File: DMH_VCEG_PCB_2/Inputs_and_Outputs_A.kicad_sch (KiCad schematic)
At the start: 43 parts, among them J1 TS_Jack_6.35mm_Sw, J10 TS_Jack_6.35mm_Sw, J2 TS_Jack_6.35mm_Sw, J200 IDC_02x08, J21 Conn_01x10_PinHeader, J22 Conn_01x10_PinHeader, J23 Conn_01x10_PinHeader, J24 Conn_01x06_PinHeader, J3 TS_Jack_6.35mm_Sw, J4 TS_Jack_6.35mm_Sw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

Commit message: Synced changes to PCB 2
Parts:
- added R197: 68k, Resistor_THT:R_Axial_DIN0207_L6.3mm_D2.5mm_P7.62mm_Horizontal, symbol Device:R_US
- added R198: 100k, Resistor_THT:R_Axial_DIN0207_L6.3mm_D2.5mm_P7.62mm_Horizontal, symbol Device:R_US
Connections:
- net +12V: now also R197.1
- net GND: now also R198.2; no longer U8.12 (+)
- new net: R197.2, R198.1, U8.12 (+)
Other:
- moved on the sheet: R88, U8D

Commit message: PCB 2 routing in progress
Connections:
- net Att CV A: no longer J23.3 (Pin_3)
- net Dec CV A: no longer J23.6 (Pin_6)
- net Rel CV A: no longer J23.10 (Pin_10)
- net Sus CV A: no longer J23.7 (Pin_7)
- no-connect marks 1 -> 5
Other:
- moved on the sheet: J23C, J23F, J23G, J23J
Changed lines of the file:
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@@
 	)
 	(junction
-		(at 146.05 34.29)
-		(diameter 0)
-		(color 0 0 0 0)
-	)
-	(junction
 		(at 171.45 163.83)
 		(diameter 0)
@@
 	)
 	(junction
-		(at 146.05 129.54)
-		(diameter 0)
-		(color 0 0 0 0)
-	)
-	(junction
 		(at 86.36 273.05)
 		(diameter 0)
@@
 	)
 	(junction
-		(at 146.05 66.04)
-		(diameter 0)
-		(color 0 0 0 0)
-	)
-	(junction
 		(at 115.57 63.5)
 		(diameter 0)
@@
 	)
 	(junction
-		(at 146.05 97.79)
-		(diameter 0)
-		(color 0 0 0 0)
-	)
-	(junction
 		(at 88.9 127)
 		(diameter 0)
@@
 	)
 	(no_connect
+		(at 146.05 127)
+	)
+	(no_connect
+		(at 146.05 95.25)
+	)
+	(no_connect
+		(at 146.05 31.75)
+	)
+	(no_connect
 		(at 66.04 257.81)
 	)
+	(no_connect
+		(at 146.05 63.5)
+	)
 	(wire
 		(pts
-			(xy 138.43 34.29) (xy 146.05 34.29)
+			(xy 138.43 34.29) (xy 158.75 34.29)
 		)
 		(stroke
@@
 	(wire
 		(pts
-			(xy 146.05 129.54) (xy 158.75 129.54)
+			(xy 138.43 129.54) (xy 158.75 129.54)
 		)
 		(stroke
@@
 	(wire
 		(pts
-			(xy 146.05 34.29) (xy 158.75 34.29)
-		)
-		(stroke
-			(width 0)
-			(type default)
-		)
-	)
-	(wire
-		(pts
 			(xy 152.4 246.38) (xy 176.53 246.38)
 		)
@@
 	(wire
 		(pts
-			(xy 138.43 129.54) (xy 146.05 129.54)
-		)
-		(stroke
-			(width 0)
-			(type default)
-		)
-	)
-	(wire
-		(pts
 			(xy 127 49.53) (xy 127 46.99)
 		)
@@
 	(wire
 		(pts
-			(xy 138.43 97.79) (xy 146.05 97.79)
-		)
-		(stroke
-			(width 0)
-			(type default)
-		)
-	)
-	(wire
-		(pts
-			(xy 138.43 66.04) (xy 146.05 66.04)
-		)
-		(stroke
-			(width 0)
-			(type default)
-		)
-	)
-	(wire
-		(pts
 			(xy 48.26 170.18) (xy 58.42 170.18)
 		)
@@
 	(wire
 		(pts
-			(xy 146.05 66.04) (xy 158.75 66.04)
+			(xy 138.43 66.04) (xy 158.75 66.04)
 		)
 		(stroke
@@
 	(wire
 		(pts
-			(xy 146.05 97.79) (xy 158.75 97.79)
+			(xy 138.43 97.79) (xy 158.75 97.79)
 		)
 		(stroke
@@
 	(symbol
 		(lib_id "SynthStuff:Conn_01x10_PinHeader")
-		(at 146.05 124.46 270)
+		(at 146.05 121.92 270)
 		(unit 10)
 		(exclude_from_sim no)
@@
 		(fields_autoplaced yes)
 		(property "Reference" "J23"
-			(at 147.32 125.0949 90)
+			(at 147.32 122.5549 90)
 			(effects
 				(font
@@
 		)
 		(property "Value" "Conn_01x10_PinHeader"
-			(at 143.51 124.46 0)
+			(at 143.51 121.92 0)
 			(effects
 				(font
@@
 		)
 		(property "Footprint" "Connector_PinSocket_2.54mm:PinSocket_1x10_P2.54mm_Vertical"
-			(at 146.05 124.46 0)
+			(at 146.05 121.92 0)
 			(effects
 				(font
@@
 		)
 		(property "Datasheet" "~"
-			(at 146.05 124.46 0)
+			(at 146.05 121.92 0)
 			(effects
 				(font
@@
 		)
 		(property "Description" "Generic connector, single row, 01x10"
-			(at 146.05 124.46 0)
+			(at 146.05 121.92 0)
 			(effects
 				(font
@@
 	(symbol
 		(lib_id "SynthStuff:Conn_01x10_PinHeader")
-		(at 146.05 29.21 270)
+		(at 146.05 26.67 270)
 		(unit 3)
 		(exclude_from_sim no)
@@
 		(fields_autoplaced yes)
 		(property "Reference" "J23"
-			(at 147.32 29.8449 90)
+			(at 147.32 27.3049 90)
 			(effects
 				(font
@@
 		)
 		(property "Value" "Conn_01x10_PinHeader"
-			(at 143.51 29.21 0)
+			(at 143.51 26.67 0)
 			(effects
 				(font
@@
 		)
 		(property "Footprint" "Connector_PinSocket_2.54mm:PinSocket_1x10_P2.54mm_Vertical"
-			(at 146.05 29.21 0)
+			(at 146.05 26.67 0)
 			(effects
 				(font
@@
 		)
 		(property "Datasheet" "~"
-			(at 146.05 29.21 0)
+			(at 146.05 26.67 0)
 			(effects
 				(font
@@
 		)
 		(property "Description" "Generic connector, single row, 01x10"
-			(at 146.05 29.21 0)
+			(at 146.05 26.67 0)
 			(effects
 				(font
@@
 	(symbol
 		(lib_id "SynthStuff:Conn_01x10_PinHeader")
-		(at 146.05 60.96 270)
+		(at 146.05 58.42 270)
 		(unit 6)
 		(exclude_from_sim no)
@@
 		(fields_autoplaced yes)
 		(property "Reference" "J23"
-			(at 147.32 61.5949 90)
+			(at 147.32 59.0549 90)
 			(effects
 				(font
@@
 		)
 		(property "Value" "Conn_01x10_PinHeader"
-			(at 143.51 60.96 0)
+			(at 143.51 58.42 0)
 			(effects
 				(font
@@
 		)
 		(property "Footprint" "Connector_PinSocket_2.54mm:PinSocket_1x10_P2.54mm_Vertical"
-			(at 146.05 60.96 0)
+			(at 146.05 58.42 0)
 			(effects
 				(font
@@
 		)
 		(property "Datasheet" "~"
-			(at 146.05 60.96 0)
+			(at 146.05 58.42 0)
 			(effects
 				(font
@@
 		)
 		(property "Description" "Generic connector, single row, 01x10"
-			(at 146.05 60.96 0)
+			(at 146.05 58.42 0)
 			(effects
 				(font
@@
 	(symbol
 		(lib_id "SynthStuff:Conn_01x10_PinHeader")
-		(at 146.05 92.71 270)
+		(at 146.05 90.17 270)
 		(unit 7)
 		(exclude_from_sim no)
@@
 		(fields_autoplaced yes)
 		(property "Reference" "J23"
-			(at 147.32 93.3449 90)
+			(at 147.32 90.8049 90)
 			(effects
 				(font
@@
 		)
 		(property "Value" "Conn_01x10_PinHeader"
-			(at 143.51 92.71 0)
+			(at 143.51 90.17 0)
 			(effects
 				(font
@@
 		)
 		(property "Footprint" "Connector_PinSocket_2.54mm:PinSocket_1x10_P2.54mm_Vertical"
-			(at 146.05 92.71 0)
+			(at 146.05 90.17 0)
 			(effects
 				(font
@@
 		)
 		(property "Datasheet" "~"
-			(at 146.05 92.71 0)
+			(at 146.05 90.17 0)
 			(effects
 				(font
@@
 		)
 		(property "Description" "Generic connector, single row, 01x10"
-			(at 146.05 92.71 0)
+			(at 146.05 90.17 0)
 			(effects
 				(font

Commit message: Restarted component placing on Main
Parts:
- removed unit 10 of J23
- removed unit 3 of J23
- removed unit 6 of J23
- removed unit 7 of J23
- renumbered J23 to J22
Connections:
- net Rel CV A: now also U21.8; no longer U21.14
- net SG Out A: now also J22.4 (Pin_4); no longer J22.2 (Pin_2)
- net Sus CV A: now also U21.14; no longer U21.8
- net at RV18.2: now also U21.10 (+); no longer U21.12 (+)
- net at R87.2, RV17.1: now also U21.9 (-); no longer U21.13 (-)
- net at J4.T, R87.1, RV18.3: now also J23.8 (Pin_8); no longer J23.9 (Pin_9)
- net at J3.T, R86.1, RV16.3: now also J23.3 (Pin_3); no longer J23.8 (Pin_8)
- net at R86.2, RV15.1: now also U21.13 (-); no longer U21.9 (-)
- net at J1.T, R84.1, RV12.3: now also J22.2 (Pin_2); no longer J22.4 (Pin_4)
- net at RV16.2: now also U21.12 (+); no longer U21.10 (+)
- no-connect marks 5 -> 1

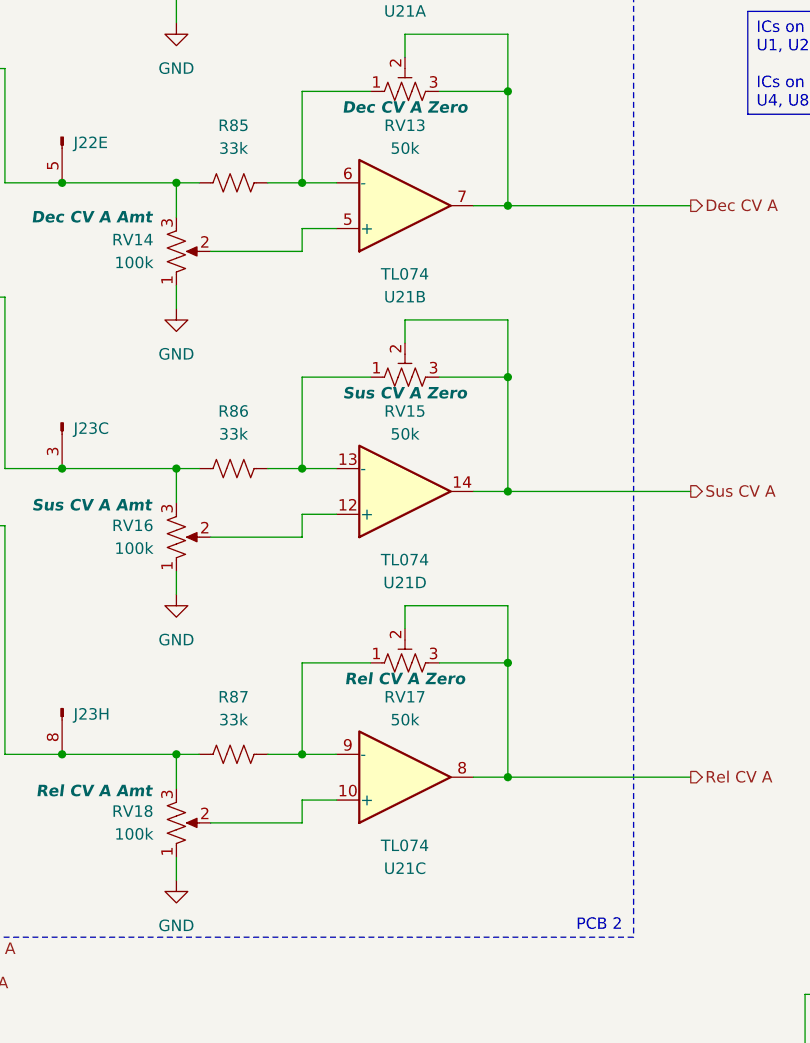
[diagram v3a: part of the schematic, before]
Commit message: PCB 2 placement in progress
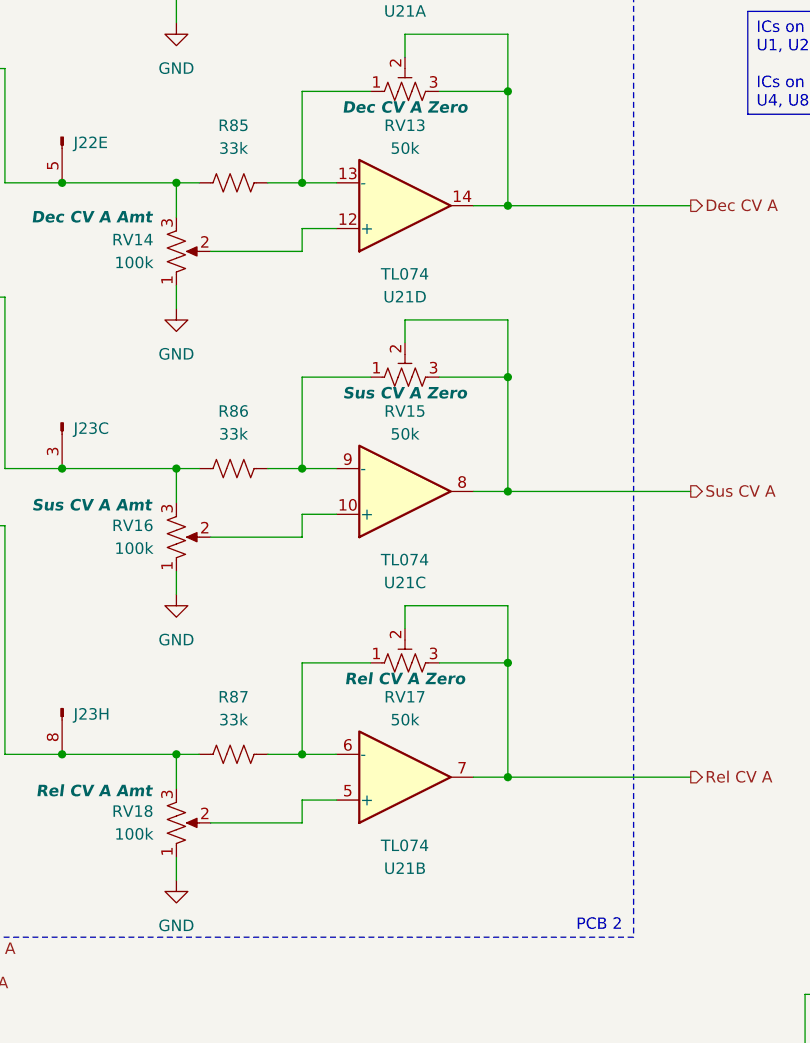
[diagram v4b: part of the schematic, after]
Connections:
- net Dec CV A: now also U21.14; no longer U21.7
- net Rel CV A: now also U21.7; no longer U21.8
- net Sus CV A: now also U21.8; no longer U21.14
- net at RV18.2: now also U21.5 (+); no longer U21.10 (+)
- net at R87.2, RV17.1: now also U21.6 (-); no longer U21.9 (-)
- net at R86.2, RV15.1: now also U21.9 (-); no longer U21.13 (-)
- net at RV14.2: now also U21.12 (+); no longer U21.5 (+)
- net at R85.2, RV13.1: now also U21.13 (-); no longer U21.6 (-)
- net at RV16.2: now also U21.10 (+); no longer U21.12 (+)
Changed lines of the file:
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@@
 		(at 127 129.54 0)
 		(mirror x)
-		(unit 3)
+		(unit 2)
 		(exclude_from_sim no)
 		(in_bom yes)
@@
 				(path "/58f4306d-5387-4983-bb08-41a2313fd315/ce3fef8b-9f1d-4178-b50b-4a046c030679"
 					(reference "U21")
-					(unit 3)
+					(unit 2)
 				)
 			)
@@
 		(at 127 66.04 0)
 		(mirror x)
-		(unit 2)
+		(unit 4)
 		(exclude_from_sim no)
 		(in_bom yes)
@@
 				(path "/58f4306d-5387-4983-bb08-41a2313fd315/ce3fef8b-9f1d-4178-b50b-4a046c030679"
 					(reference "U21")
-					(unit 2)
+					(unit 4)
 				)
 			)
@@
 		(at 127 97.79 0)
 		(mirror x)
-		(unit 4)
+		(unit 3)
 		(exclude_from_sim no)
 		(in_bom yes)
@@
 				(path "/58f4306d-5387-4983-bb08-41a2313fd315/ce3fef8b-9f1d-4178-b50b-4a046c030679"
 					(reference "U21")
-					(unit 4)
+					(unit 3)
 				)
 			)

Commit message: PCB 2 placement done
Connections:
- net SG Out A: now also J22.5 (Pin_5); no longer J22.4 (Pin_4)
- net at J2.T, R85.1, RV14.3: now also J22.4 (Pin_4); no longer J22.5 (Pin_5)
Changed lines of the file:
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@@
 		(lib_id "SynthStuff:Conn_01x10_PinHeader")
 		(at 144.78 170.18 270)
-		(unit 4)
+		(unit 5)
 		(exclude_from_sim no)
 		(in_bom yes)
@@
 				(path "/58f4306d-5387-4983-bb08-41a2313fd315/ce3fef8b-9f1d-4178-b50b-4a046c030679"
 					(reference "J22")
-					(unit 4)
+					(unit 5)
 				)
 			)
@@
 		(lib_id "SynthStuff:Conn_01x10_PinHeader")
 		(at 88.9 58.42 270)
-		(unit 5)
+		(unit 4)
 		(exclude_from_sim no)
 		(in_bom yes)
@@
 				(path "/58f4306d-5387-4983-bb08-41a2313fd315/ce3fef8b-9f1d-4178-b50b-4a046c030679"
 					(reference "J22")
-					(unit 5)
-				)
-			)
+					(unit 4)
+				)
+			)

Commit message: Found mistake with SG Out offset resistors
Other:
- note added: "Must be inverted"
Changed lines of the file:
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@@
+	)
+	(rectangle
+		(start 118.11 187.96)
+		(end 135.89 193.04)
+		(stroke
+			(width 0)
+			(type default)
+		)
+		(fill
+			(type none)
+		)
 	)
 	(rectangle
@@
 		(effects
 			(font
+				(size 1.27 1.27)
+			)
+		)
+	)
+	(text "Must be inverted"
+		(exclude_from_sim no)
+		(at 128.016 186.69 0)
+		(effects
+			(font
